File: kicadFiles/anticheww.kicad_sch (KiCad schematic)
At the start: 372 parts, among them J1 TYPE-C-31-M12_13, Q1 AO3401A, Q2 DTC123JKAT146, SW1 ESC, SW10 9, SW11 0, SW12 MINUS, SW13 PLUS, SW14 LBKSP, SW15 RBKSP, SW16 2U_BKSP, SW17 TAB, SW18 Q, SW19 W, SW2 1, SW20 E, SW21 R, SW22 T, SW23 Y, SW24 U, SW25 I, SW26 O, SW27 P, SW28 LBRKT, SW29 RBRKT, SW3 2, SW30 BKSLSH, SW31 PGDN, SW32 ISO_ENTER, SW33 CAPS, SW34 A, SW35 S, SW36 D, SW37 F, SW38 G, SW39 H, SW4 3, SW40 J, SW41 K, SW42 L, SW43 COLON, SW44 QUOTE, SW45 ENTER, SW46 HOME, SW47 PGUP, SW48 STEPPED_CAPS, SW49 ISO_TILDE, SW5 4, SW50 LSHFT, SW51 ISO_BKLSH, SW52 Z, SW53 X, SW54 C, SW55 V, SW56 B, SW57 N, SW58 M, SW59 COMMA, SW6 5, SW60 DOT, SW61 SLSH, SW62 175_RSHFT, SW63 UP, SW64 END, SW65 ISO_LSHFT, SW66 LCTRL, SW67 LGUI, SW68 LALT, SW69 SPC, SW7 6, SW70 RALT, SW71 RGUI, SW72 RCTRL, SW73 LEFT, SW74 DOWN, SW75 RIGHT, SW76 LCTRL, SW77 LGUI, SW78 LALT, SW79 SPC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

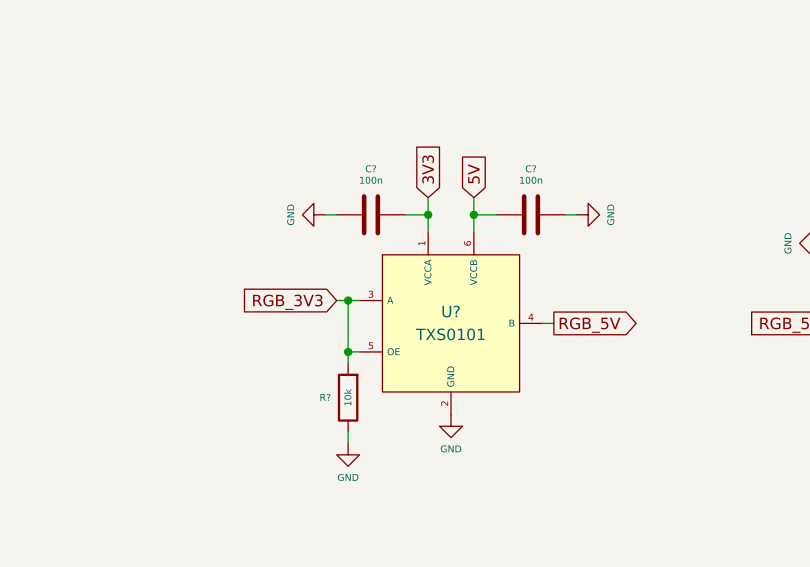
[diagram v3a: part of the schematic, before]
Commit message: Add level shifter circuit to PCB
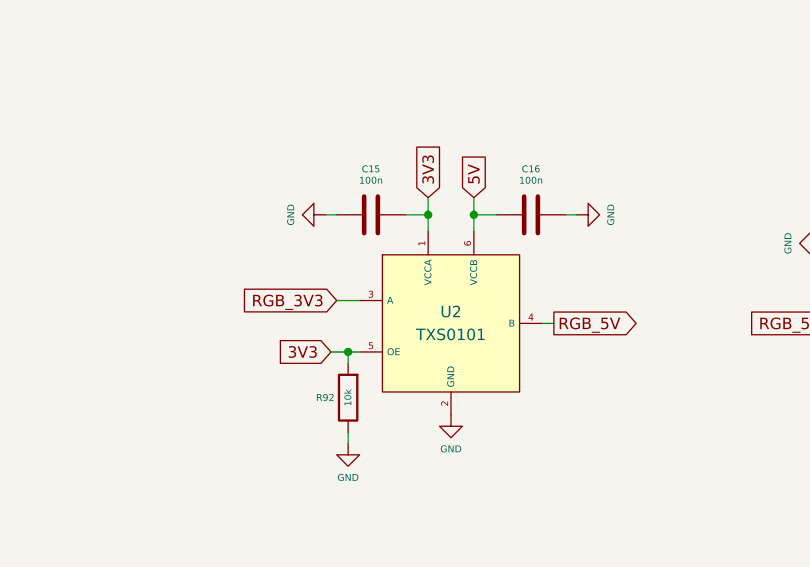
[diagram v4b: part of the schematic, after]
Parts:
- gave numbers to parts that had none: 4
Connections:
- net 3V3: now also R92.2, U2.5 (OE)
- net RGB_3V3: no longer R92.2, U2.5 (OE)
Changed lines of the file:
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@@
   (junction (at 473.71 63.5) (diameter 0) (color 0 0 0 0))
   (junction (at 482.6 54.61) (diameter 0) (color 0 0 0 0))
-  (junction (at 501.015 283.21) (diameter 0) (color 0 0 0 0))
   (junction (at 501.015 288.925) (diameter 0) (color 0 0 0 0))
   (junction (at 509.905 273.685) (diameter 0) (color 0 0 0 0))
@@
     (stroke (width 0) (type solid) (color 0 0 0 0))
   )
-  (wire (pts (xy 501.015 283.21) (xy 499.745 283.21))
+  (wire (pts (xy 499.11 288.925) (xy 501.015 288.925))
     (stroke (width 0) (type solid) (color 0 0 0 0))
   )
-  (wire (pts (xy 501.015 283.21) (xy 502.285 283.21))
-    (stroke (width 0) (type solid) (color 0 0 0 0))
-  )
-  (wire (pts (xy 501.015 288.925) (xy 501.015 283.21))
+  (wire (pts (xy 499.745 283.21) (xy 502.285 283.21))
     (stroke (width 0) (type solid) (color 0 0 0 0))
   )
@@
     (effects (font (size 0.762 0.762)) (justify left))
   )
+  (global_label "3V3" (shape input) (at 499.11 288.925 180)
+    (effects (font (size 1.27 1.27)) (justify right))
+  )
   (global_label "RGB_3V3" (shape input) (at 499.745 283.21 180)
     (effects (font (size 1.27 1.27)) (justify right))
@@
   (symbol (lib_id "power:GND") (at 498.475 273.685 270) (unit 1)
     (in_bom yes) (on_board yes)
-    (property "Reference" "#PWR?" (id 0) (at 492.125 273.685 0)
+    (property "Reference" "#PWR0118" (id 0) (at 492.125 273.685 0)
       (effects (font (size 1.27 1.27)) hide)
     )
@@
   (symbol (lib_id "power:GND") (at 501.015 299.085 0) (unit 1)
     (in_bom yes) (on_board yes)
-    (property "Reference" "#PWR?" (id 0) (at 501.015 305.435 0)
+    (property "Reference" "#PWR0116" (id 0) (at 501.015 305.435 0)
       (effects (font (size 1.27 1.27)) hide)
     )
@@
   (symbol (lib_id "power:GND") (at 512.445 295.91 0) (unit 1)
     (in_bom yes) (on_board yes)
-    (property "Reference" "#PWR?" (id 0) (at 512.445 302.26 0)
+    (property "Reference" "#PWR0119" (id 0) (at 512.445 302.26 0)
       (effects (font (size 1.27 1.27)) hide)
     )
@@
   (symbol (lib_id "power:GND") (at 526.415 273.685 90) (unit 1)
     (in_bom yes) (on_board yes)
-    (property "Reference" "#PWR?" (id 0) (at 532.765 273.685 0)
+    (property "Reference" "#PWR0117" (id 0) (at 532.765 273.685 0)
       (effects (font (size 1.27 1.27)) hide)
     )
@@
   (symbol (lib_id "Device:R") (at 501.015 294.005 180) (unit 1)
     (in_bom yes) (on_board yes)
-    (property "Reference" "R?" (id 0) (at 498.475 294.005 0)
+    (property "Reference" "R92" (id 0) (at 498.475 294.005 0)
       (effects (font (size 0.762 0.762)))
     )
@@
   (symbol (lib_id "Device:C") (at 503.555 273.685 90) (unit 1)
     (in_bom yes) (on_board yes)
-    (property "Reference" "C?" (id 0) (at 503.555 268.605 90)
+    (property "Reference" "C15" (id 0) (at 503.555 268.605 90)
       (effects (font (size 0.762 0.762)))
     )
@@
   (symbol (lib_id "Device:C") (at 521.335 273.685 90) (unit 1)
     (in_bom yes) (on_board yes)
-    (property "Reference" "C?" (id 0) (at 521.335 268.605 90)
+    (property "Reference" "C16" (id 0) (at 521.335 268.605 90)
       (effects (font (size 0.762 0.762)))
     )
@@
   (symbol (lib_id "acheronSymbols:TXS0101") (at 512.445 285.75 0) (unit 1)
     (in_bom yes) (on_board yes)
-    (property "Reference" "U?" (id 0) (at 512.445 284.48 0))
+    (property "Reference" "U2" (id 0) (at 512.445 284.48 0))
     (property "Value" "TXS0101" (id 1) (at 512.445 287.02 0))
     (property "Footprint" "acheron_Components:SOT-23-6" (id 2) (at 512.445 285.75 0)
@@
     )
     (path "/13a4c659-1c15-4b53-86e0-ca041dc591f3"
-      (reference "#PWR?") (unit 1)
-    )
-    (path "/490620fd-613d-4d43-ac4c-9b8c577bdf04"
-      (reference "#PWR?") (unit 1)
+      (reference "#PWR0116") (unit 1)
     )
     (path "/85e58f8b-f339-49c6-93a4-a7b775f45c5e"
-      (reference "#PWR?") (unit 1)
+      (reference "#PWR0117") (unit 1)
     )
     (path "/d7e70bbe-15f5-4ad0-a9d7-235a66e904c0"
-      (reference "#PWR?") (unit 1)
+      (reference "#PWR0118") (unit 1)
+    )
+    (path "/490620fd-613d-4d43-ac4c-9b8c577bdf04"
+      (reference "#PWR0119") (unit 1)
     )
     (path "/ae5774e2-b57d-45f9-8f18-00fe968ff91c"
@@
       (reference "C14") (unit 1)
     )
-    (path "/050c44df-f928-4f34-a0ac-e2f59ee6d0c3"
-      (reference "C?") (unit 1)
-    )
     (path "/f7ac074f-f911-44dc-aa62-2d288e94e739"
-      (reference "C?") (unit 1)
+      (reference "C15") (unit 1)
+    )
+    (path "/050c44df-f928-4f34-a0ac-e2f59ee6d0c3"
+      (reference "C16") (unit 1)
     )
     (path "/543a7d54-a886-4795-b487-5ed8576a1063"
@@
     )
     (path "/d4c265a0-89ce-416a-9ca9-e8c94d13e1e4"
-      (reference "R?") (unit 1)
+      (reference "R92") (unit 1)
     )
     (path "/983f5a57-4b10-4c42-94d3-0d9551b32e38"
@@
     )
     (path "/a724a7f8-7295-42d3-bdde-b64d2a94622f"
-      (reference "U?") (unit 1)
+      (reference "U2") (unit 1)
     )
   )

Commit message: Added split space and 2.75 split RShift support
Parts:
- added D85, D86: 1N4148W, acheron_Components:D_SOD-123, symbol Device:D
- added LED81, LED82, LED83, LED84, LED85, LED86, LED87: LED, acheron_Components:LED_THT_2.54mm, symbol acheronSymbols:LED
- added R93, R94: 420R, Resistor_SMD:R_0805_2012Metric, symbol Device:R
- added SW80: 275_RSHFT, acheron_MX_SolderMask:MX275, symbol acheronSymbols:MXSwitch
- added SW81, SW86: 275_SPC, acheron_MX_SolderMask:MX275R, symbol acheronSymbols:MXSwitch
- added SW82: 125_SPC, acheron_MX_SolderMask:MX125, symbol acheronSymbols:MXSwitch
- added SW83, SW84: 225_SPC, acheron_MX_SolderMask:MX225R, symbol acheronSymbols:MXSwitch
- added SW85: SPC, acheron_MX_SolderMask:MX125, symbol acheronSymbols:MXSwitch
- added SW87, SW88, SW89, SW90: Rotary_Encoder_Switch_Chassis, acheron_Hardware:ALPS_EC11E, symbol acheronSymbols:Rotary_Encoder_Switch_Chassis
- GR3: value Warning Sign (ANSI Enter + ISO Backslash) -> Warning Sign (ANSI Enter + ISO Backslash LED)
- SW45: footprint acheron_MX_SolderMask:MX225 -> acheron_MX_SolderMask:MX225R
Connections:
- net GND: now also LED81.K, LED82.K, LED83.K, LED84.K, LED85.K, LED86.K, LED87.K
- net S4: now also SW79.1 (Col), SW82.2 (Row), SW85.2 (Row); no longer SW79.2 (Row)
- net at Q1.3 (D), R10.2, R11.2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: now also R93.2, R94.2
- net at SW13.1 (Col), SW29.1 (Col), SW45.1 (Col)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: now also SW80.1 (Col)
- net at SW22.1 (Col), SW38.1 (Col), SW55.1 (Col)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: now also SW79.2 (Row), SW82.1 (Col), SW85.1 (Col); no longer SW79.1 (Col)
- net at SW23.1 (Col), SW39.1 (Col), SW56.1 (Col)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: now also SW83.1 (Col), SW86.1 (Col)
- net at D61.1 (K), D62.1 (K), D63.1 (K)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: now also D85.1 (K), D86.1 (K)
- net at LED62.A, R75.1: now also LED81.A
- net at SW21.1 (Col), SW37.1 (Col), SW5.1 (Col)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: now also SW81.1 (Col), SW84.1 (Col)
- net at LED71.A, LED72.A, R81.1: now also LED82.A, LED83.A
- net at D58.2 (A), SW62.2 (Row): now also SW80.2 (Row)
- new net: LED84.A, LED85.A, R93.1
- new net: LED86.A, LED87.A, R94.1
- new net S5: D85.2 (A), D86.2 (A), SW81.2 (Row), SW83.2 (Row), SW84.2 (Row), SW86.2 (Row)
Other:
- moved on the sheet: LED63, LED64, LED71, LED72, LED73, LED74, LED75, LED76, LED77, LED78, LED79, LED80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

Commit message: Route most components
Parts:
- removed LED80: LED, acheron_Components:LED_THT_2.54mm, symbol acheronSymbols:LED
- removed R89: 420R, Resistor_SMD:R_0805_2012Metric, symbol Device:R
- added C17, C18, C23: 100n, Capacitor_SMD:C_0805_2012Metric, symbol Device:C_Small
- added C19, C20, C21, C29: 100n, Capacitor_SMD:C_0402_1005Metric, symbol Device:C_Small
- added C22, C30: 4.7u, Capacitor_SMD:C_0402_1005Metric, symbol Device:C_Small
- added C24, C25: 1u, acheron_Components:CP_EIA-3216-10_Kemet-I_Pad1.58x1.35mm_HandSolder, symbol Device:CP1
- added C26: 1u, Capacitor_SMD:C_0402_1005Metric, symbol Device:C_Small
- added C27: 10n, Capacitor_SMD:C_0402_1005Metric, symbol Device:C_Small
- added C28: 100u, Capacitor_SMD:C_0805_2012Metric, symbol Device:C_Small
- added D87: RB060M-60TR, acheron_Components:D_SOD-123, symbol Device:D_Schottky
- added D88: 1N4148W, acheron_Components:D_SOD-123, symbol Device:D
- added F1: Polyfuse, Fuse:Fuse_1812_4532Metric, symbol Device:Polyfuse
- added J2: ARM JTAG, acheron_Connectors:Conn_ARM_JTAG_SWD_6, symbol Connector_Generic:Conn_02x03_Odd_Even
- added Q3: DTC123JKAT146, Package_TO_SOT_SMD:SOT-23, symbol acheronSymbols:DTC123J
- added R100, R99: 100k, acheron_Components:R_0805_2012Metric_LEDs, symbol Device:R
- added R101: 33k, Resistor_SMD:R_0805_2012Metric, symbol Device:R_Small
- added R102: 100k, Resistor_SMD:R_0805_2012Metric, symbol Device:R_Small
- added R94: 10k, acheron_Components:R_0805_2012Metric_LEDs, symbol Device:R
- added R95, R96, R97: 10k, Resistor_SMD:R_0805_2012Metric, symbol Device:R
- added R98: 100R, Resistor_SMD:R_0805_2012Metric, symbol Device:R_Small
- added S1: K2-1187SQ-A4SW-06, acheron_Hardware:K2-1187SQ-A4SW-06, symbol Switch:SW_SPST
- added U3: STM32F072-LQFP48, acheron_Components:LQFP-48_7x7mm_P0.5mm, symbol acheronSymbols:STM32F072-LQFP48
- added U4: MCP1700-3302E_SOT23, Package_TO_SOT_SMD:SOT-23, symbol Regulator_Linear:MCP1700-3302E_SOT23
- C10: renamed from C14; footprint Capacitor_SMD:C_0805_2012Metric -> acheron_Components:C_0805_2012Metric_RGB
- C11: renamed from C13; footprint Capacitor_SMD:C_0805_2012Metric -> acheron_Components:C_0805_2012Metric_RGB
- C12: footprint Capacitor_SMD:C_0805_2012Metric -> acheron_Components:C_0805_2012Metric_RGB
- C13: renamed from C11; footprint Capacitor_SMD:C_0805_2012Metric -> acheron_Components:C_0805_2012Metric_RGB
- C14: renamed from C10; footprint Capacitor_SMD:C_0805_2012Metric -> acheron_Components:C_0805_2012Metric_RGB
- C15: renamed from C9; footprint Capacitor_SMD:C_0805_2012Metric -> acheron_Components:C_0805_2012Metric_RGB
- C16: renamed from C8; footprint Capacitor_SMD:C_0805_2012Metric -> acheron_Components:C_0805_2012Metric_RGB
- C3: renamed from C1; footprint Capacitor_SMD:C_0805_2012Metric -> acheron_Components:C_0805_2012Metric_RGB
- C4: renamed from C2; footprint Capacitor_SMD:C_0805_2012Metric -> acheron_Components:C_0805_2012Metric_RGB
- C5: renamed from C3; footprint Capacitor_SMD:C_0805_2012Metric -> acheron_Components:C_0805_2012Metric_RGB
- C6: renamed from C4; footprint Capacitor_SMD:C_0805_2012Metric -> acheron_Components:C_0805_2012Metric_RGB
- C7: renamed from C5; footprint Capacitor_SMD:C_0805_2012Metric -> acheron_Components:C_0805_2012Metric_RGB
- C8: renamed from C6; footprint Capacitor_SMD:C_0805_2012Metric -> acheron_Components:C_0805_2012Metric_RGB
- C9: renamed from C7; footprint Capacitor_SMD:C_0805_2012Metric -> acheron_Components:C_0805_2012Metric_RGB
- R10, R11, R12, R13, R14, R15, R16, R17, R18, R19, R20, R21, R22, R23, R24, R25, R3, R4, R5, R6, R7, R8, R9: footprint Resistor_SMD:R_0805_2012Metric -> acheron_Components:R_0805_2012Metric_LEDs
- R27: renamed from R32; footprint Resistor_SMD:R_0805_2012Metric -> acheron_Components:R_0805_2012Metric_LEDs
- R28: renamed from R31; footprint Resistor_SMD:R_0805_2012Metric -> acheron_Components:R_0805_2012Metric_LEDs
- R29: renamed from R30; footprint Resistor_SMD:R_0805_2012Metric -> acheron_Components:R_0805_2012Metric_LEDs
- R30: renamed from R29; footprint Resistor_SMD:R_0805_2012Metric -> acheron_Components:R_0805_2012Metric_LEDs
- R31: renamed from R28; footprint Resistor_SMD:R_0805_2012Metric -> acheron_Components:R_0805_2012Metric_LEDs
- R32: renamed from R27; footprint Resistor_SMD:R_0805_2012Metric -> acheron_Components:R_0805_2012Metric_LEDs
- R33: renamed from R26; footprint Resistor_SMD:R_0805_2012Metric -> acheron_Components:R_0805_2012Metric_LEDs
- R34: renamed from R33; footprint Resistor_SMD:R_0805_2012Metric -> acheron_Components:R_0805_2012Metric_LEDs
- R35: renamed from R34; footprint Resistor_SMD:R_0805_2012Metric -> acheron_Components:R_0805_2012Metric_LEDs
- R36: renamed from R35; footprint Resistor_SMD:R_0805_2012Metric -> acheron_Components:R_0805_2012Metric_LEDs
- R37: renamed from R36; footprint Resistor_SMD:R_0805_2012Metric -> acheron_Components:R_0805_2012Metric_LEDs
- R38: renamed from R37; footprint Resistor_SMD:R_0805_2012Metric -> acheron_Components:R_0805_2012Metric_LEDs
- R39: renamed from R38; footprint Resistor_SMD:R_0805_2012Metric -> acheron_Components:R_0805_2012Metric_LEDs
- R40: renamed from R39; footprint Resistor_SMD:R_0805_2012Metric -> acheron_Components:R_0805_2012Metric_LEDs
- R41: renamed from R40; footprint Resistor_SMD:R_0805_2012Metric -> acheron_Components:R_0805_2012Metric_LEDs
- R42: renamed from R41; footprint Resistor_SMD:R_0805_2012Metric -> acheron_Components:R_0805_2012Metric_LEDs
- R43: renamed from R42; footprint Resistor_SMD:R_0805_2012Metric -> acheron_Components:R_0805_2012Metric_LEDs
- R44: renamed from R43; footprint Resistor_SMD:R_0805_2012Metric -> acheron_Components:R_0805_2012Metric_LEDs
- R45: renamed from R44; footprint Resistor_SMD:R_0805_2012Metric -> acheron_Components:R_0805_2012Metric_LEDs
- R46: renamed from R45; footprint Resistor_SMD:R_0805_2012Metric -> acheron_Components:R_0805_2012Metric_LEDs
- R47: renamed from R46; footprint Resistor_SMD:R_0805_2012Metric -> acheron_Components:R_0805_2012Metric_LEDs
- R48: renamed from R47; footprint Resistor_SMD:R_0805_2012Metric -> acheron_Components:R_0805_2012Metric_LEDs
- R49: renamed from R48; footprint Resistor_SMD:R_0805_2012Metric -> acheron_Components:R_0805_2012Metric_LEDs
- R50: renamed from R49; footprint Resistor_SMD:R_0805_2012Metric -> acheron_Components:R_0805_2012Metric_LEDs
- R51: renamed from R50; footprint Resistor_SMD:R_0805_2012Metric -> acheron_Components:R_0805_2012Metric_LEDs
- R52: renamed from R51; footprint Resistor_SMD:R_0805_2012Metric -> acheron_Components:R_0805_2012Metric_LEDs
- R53: renamed from R52; footprint Resistor_SMD:R_0805_2012Metric -> acheron_Components:R_0805_2012Metric_LEDs
- R54: renamed from R53; footprint Resistor_SMD:R_0805_2012Metric -> acheron_Components:R_0805_2012Metric_LEDs
- R55: renamed from R54; footprint Resistor_SMD:R_0805_2012Metric -> acheron_Components:R_0805_2012Metric_LEDs
- R56: renamed from R55; footprint Resistor_SMD:R_0805_2012Metric -> acheron_Components:R_0805_2012Metric_LEDs
- R57: renamed from R56; footprint Resistor_SMD:R_0805_2012Metric -> acheron_Components:R_0805_2012Metric_LEDs
- R58: renamed from R57; footprint Resistor_SMD:R_0805_2012Metric -> acheron_Components:R_0805_2012Metric_LEDs
- R59: renamed from R58; footprint Resistor_SMD:R_0805_2012Metric -> acheron_Components:R_0805_2012Metric_LEDs
- R60: renamed from R59; footprint Resistor_SMD:R_0805_2012Metric -> acheron_Components:R_0805_2012Metric_LEDs
- R61: renamed from R60; footprint Resistor_SMD:R_0805_2012Metric -> acheron_Components:R_0805_2012Metric_LEDs
- R62: renamed from R61; footprint Resistor_SMD:R_0805_2012Metric -> acheron_Components:R_0805_2012Metric_LEDs
- R63: renamed from R62; footprint Resistor_SMD:R_0805_2012Metric -> acheron_Components:R_0805_2012Metric_LEDs
- R64: renamed from R63; footprint Resistor_SMD:R_0805_2012Metric -> acheron_Components:R_0805_2012Metric_LEDs
- R65: renamed from R64; footprint Resistor_SMD:R_0805_2012Metric -> acheron_Components:R_0805_2012Metric_LEDs
- R66: renamed from R65; footprint Resistor_SMD:R_0805_2012Metric -> acheron_Components:R_0805_2012Metric_LEDs
- R67: renamed from R66; footprint Resistor_SMD:R_0805_2012Metric -> acheron_Components:R_0805_2012Metric_LEDs
- R68: renamed from R67; footprint Resistor_SMD:R_0805_2012Metric -> acheron_Components:R_0805_2012Metric_LEDs
- R69: renamed from R68; footprint Resistor_SMD:R_0805_2012Metric -> acheron_Components:R_0805_2012Metric_LEDs
- R70: renamed from R69; footprint Resistor_SMD:R_0805_2012Metric -> acheron_Components:R_0805_2012Metric_LEDs
- R71: renamed from R70; footprint Resistor_SMD:R_0805_2012Metric -> acheron_Components:R_0805_2012Metric_LEDs
- R72: renamed from R71; footprint Resistor_SMD:R_0805_2012Metric -> acheron_Components:R_0805_2012Metric_LEDs
- R73: renamed from R72; footprint Resistor_SMD:R_0805_2012Metric -> acheron_Components:R_0805_2012Metric_LEDs
- R74: renamed from R73; footprint Resistor_SMD:R_0805_2012Metric -> acheron_Components:R_0805_2012Metric_LEDs
- R75: renamed from R74; footprint Resistor_SMD:R_0805_2012Metric -> acheron_Components:R_0805_2012Metric_LEDs
- R76: renamed from R75; footprint Resistor_SMD:R_0805_2012Metric -> acheron_Components:R_0805_2012Metric_LEDs
- R77: renamed from R76; footprint Resistor_SMD:R_0805_2012Metric -> acheron_Components:R_0805_2012Metric_LEDs
- R78: renamed from R77; footprint Resistor_SMD:R_0805_2012Metric -> acheron_Components:R_0805_2012Metric_LEDs
- R79: renamed from R78; footprint Resistor_SMD:R_0805_2012Metric -> acheron_Components:R_0805_2012Metric_LEDs
- R80: renamed from R79; footprint Resistor_SMD:R_0805_2012Metric -> acheron_Components:R_0805_2012Metric_LEDs
- R81: renamed from R80; footprint Resistor_SMD:R_0805_2012Metric -> acheron_Components:R_0805_2012Metric_LEDs
- R82: renamed from R93; footprint Resistor_SMD:R_0805_2012Metric -> acheron_Components:R_0805_2012Metric_LEDs
- R83: renamed from R81; footprint Resistor_SMD:R_0805_2012Metric -> acheron_Components:R_0805_2012Metric_LEDs
- R84: renamed from R94; footprint Resistor_SMD:R_0805_2012Metric -> acheron_Components:R_0805_2012Metric_LEDs
- R85: renamed from R82; footprint Resistor_SMD:R_0805_2012Metric -> acheron_Components:R_0805_2012Metric_LEDs
- R86: renamed from R83; footprint Resistor_SMD:R_0805_2012Metric -> acheron_Components:R_0805_2012Metric_LEDs
- R87: renamed from R84; footprint Resistor_SMD:R_0805_2012Metric -> acheron_Components:R_0805_2012Metric_LEDs
- R88: renamed from R85; footprint Resistor_SMD:R_0805_2012Metric -> acheron_Components:R_0805_2012Metric_LEDs
- R89: renamed from R86; footprint Resistor_SMD:R_0805_2012Metric -> acheron_Components:R_0805_2012Metric_LEDs
- R90: renamed from R87; footprint Resistor_SMD:R_0805_2012Metric -> acheron_Components:R_0805_2012Metric_LEDs
- R91: renamed from R88; footprint Resistor_SMD:R_0805_2012Metric -> acheron_Components:R_0805_2012Metric_LEDs
- renumbered C15 to C1, C16 to C2, D85 to D71, D86 to D72, D71 to D73, D72 to D74, D73 to D75, D74 to D76, D75 to D77, D76 to D78, D77 to D79, D84 to D80, D83 to D81, D81 to D83, D80 to D84, D79 to D85, D78 to D86, LED81 to LED49, LED49 to LED50, LED50 to LED51, LED51 to LED52, LED52 to LED53, LED53 to LED54, LED54 to LED55, LED55 to LED56, LED56 to LED57, LED57 to LED58, LED58 to LED59, LED59 to LED60, LED60 to LED61, LED61 to LED62, LED62 to LED63, LED63 to LED64, LED64 to LED65, LED65 to LED66, LED66 to LED67, LED67 to LED68, LED68 to LED69, LED69 to LED70, LED70 to LED71, LED84 to LED72, LED85 to LED73, LED71 to LED74, LED72 to LED75, LED82 to LED76, LED83 to LED77, LED86 to LED78, LED87 to LED79, LED73 to LED80, LED74 to LED81, LED75 to LED82, LED76 to LED83, LED77 to LED84, LED78 to LED85, LED79 to LED86, R92 to R26, R90 to R92, R91 to R93, SW87 to SW16, SW16 to SW17, SW88 to SW18, SW17 to SW19, SW18 to SW20, SW19 to SW21, SW20 to SW22, SW21 to SW23, SW22 to SW24, SW23 to SW25, SW24 to SW26, SW25 to SW27, SW26 to SW28, SW27 to SW29, SW28 to SW30, SW29 to SW31, SW30 to SW32, SW31 to SW33, SW32 to SW34, SW89 to SW35, SW33 to SW36, SW34 to SW37, SW35 to SW38, SW36 to SW39, SW37 to SW40, SW38 to SW41, SW39 to SW42, SW40 to SW43, SW41 to SW44, SW42 to SW45, SW43 to SW46, SW44 to SW47, SW45 to SW48, SW46 to SW49, SW47 to SW50, SW48 to SW51, SW49 to SW52, SW90 to SW53, SW50 to SW54, SW51 to SW55, SW52 to SW56, SW53 to SW57, SW54 to SW58, SW55 to SW59, SW56 to SW60, SW57 to SW61, SW58 to SW62, SW59 to SW63, SW60 to SW64, SW61 to SW65, SW62 to SW66, SW63 to SW67, SW64 to SW68, SW65 to SW69, SW80 to SW70, SW66 to SW71, SW67 to SW72, SW68 to SW73, SW69 to SW74, SW70 to SW75, SW71 to SW76, SW72 to SW77, SW73 to SW78, SW74 to SW79, SW75 to SW80, SW76 to SW81, SW77 to SW82, SW78 to SW83, SW79 to SW84, SW81 to SW85, SW82 to SW86, SW83 to SW87, SW84 to SW88, SW85 to SW89, SW86 to SW90, U2 to U1, U1 to U2
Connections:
- net 3V3: now also C19.1, C20.1, C21.2, C22.2, C25.1, C26.1, C27.1, C29.2, C30.2, D87.2 (A), J2.1 (Pin_1), R100.1, R94.1, R95.1, S1.1 (A), U3.1 (VBAT), U3.24 (VDD), U3.36 (VDDIO2), U3.48 (VDD), U3.9 (VDDA), U4.2 (VO)
- net 5V: now also C24.1, D87.1 (K), F1.2, R99.1, U4.3 (VI)
- net D+: now also U3.33 (USB_DP/PA12)
- net D-: now also U3.32 (USB_DM/TIM1_CH4/PA11)
- net GND: now also C17.2, C18.2, C19.2, C20.2, C21.1, C22.1, C23.2, C24.2, C25.2, C26.2, C27.2, C28.1, C29.1, C30.1, J2.5 (Pin_5), Q3.2 (E), R100.2, R102.1, R99.2, U3.23 (VSS), U3.35 (VSS), U3.47 (VSS), U3.8 (VSSA), U4.1 (GND)
- net S4: now also D71.2 (A), SW85.2 (Row), SW88.2 (Row); no longer D64.2 (A), SW74.2 (Row), SW84.1 (Col), SW86.2 (Row), SW89.2 (Row)
- net S5: now also D64.2 (A), SW74.2 (Row), SW84.1 (Col), SW86.2 (Row), SW89.2 (Row); no longer D71.2 (A), D72.2 (A), SW85.2 (Row), SW87.2 (Row), SW88.2 (Row), SW90.2 (Row)
- net VBUS: now also F1.1
- net at SW25.1 (Col), SW42.1 (Col), SW60.1 (Col)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: now also SW74.1 (Col), SW84.2 (Row), SW86.1 (Col), SW89.1 (Col); no longer SW87.1 (Col), SW90.1 (Col)
- net at SW24.1 (Col), SW41.1 (Col), SW59.1 (Col)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: no longer SW74.1 (Col), SW84.2 (Row), SW86.1 (Col), SW89.1 (Col)
- net at D84.2 (DOUT): now also D83.4 (DIN); no longer D85.4 (DIN)
- net at D84.4 (DIN): now also D85.2 (DOUT); no longer D83.2 (DOUT)
- net at D86.2 (DOUT): now also D85.4 (DIN)
- net at D86.4 (DIN): now also D79.2 (DOUT); no longer D85.2 (DOUT)
- net at D82.2 (DOUT): now also D81.4 (DIN); no longer D83.4 (DIN)
- net at D82.4 (DIN): now also D83.2 (DOUT); no longer D81.2 (DOUT)
- net at SW27.1 (Col), SW44.1 (Col), SW62.1 (Col)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: now also SW87.1 (Col), SW90.1 (Col)
- net at D80.2 (DOUT): no longer D81.4 (DIN)
- net at D80.4 (DIN): now also D81.2 (DOUT); no longer D79.2 (DOUT)
- new net: C17.1, R96.2
- new net: D88.2 (A), Q3.1 (B), S1.2 (B)
- new net: R94.2, R96.1
- new net: Q3.3 (C), R98.1
- new net: D88.1 (K), R101.1
- new net BOOT0: C28.2, R101.2, R102.2, U3.44 (BOOT0)
- new net ENCB: R95.2, R97.1
- new net NRST: C23.1, J2.3 (Pin_3), R98.2, U3.7 (NRST)
- new net ROTB: C18.1, R97.2
- new net S6: D72.2 (A), SW87.2 (Row), SW90.2 (Row)
- new net SWCLK: J2.4 (Pin_4), U3.37 (SWCLK/PA14)
- new net SWDIO: J2.2 (Pin_2), U3.34 (SWDIO/PA13)
- no-connect marks 0 -> 1
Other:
- note added: "3V3"
- note added: "HARD RESET"
- note added: "MCU"
- moved on the sheet: C10, C11, C12, C14, C15, C16, D64, D72, D80, D81, D82, D84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
